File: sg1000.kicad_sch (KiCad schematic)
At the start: 77 parts, among them CN1 Conn_01x07_Female, J1 USB-B1HSB6, J2 RCJ-014, J3 RCJ-013, Q1 2n4401, Q1c1 2n3906, SW1 Pause Key, SW2 Power Toggle, SW3 Reset Key, U1 SG-1000-Cart, U100 74HCT574, U101 74HCT574, U102 74HCT574, U103 AS6C62256-DIP, U11 AS6C62256-DIP, U12 TMS9918A, U13 74LS139, U16 74LS32, U17 74LS14, U18 74LS257, U2 SG-1000-Expansion, U21 74LS257, U3 SN76489AN, U4 74LS32, U5 27C256, U6 74LS573, U7 74LS00, U9 Z80CPU, U99 74HCT04, X2 10.73863MHz

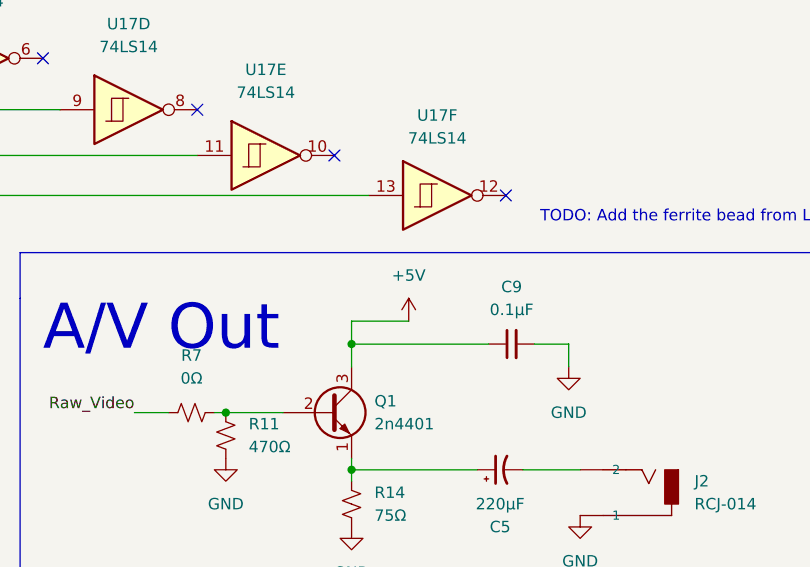
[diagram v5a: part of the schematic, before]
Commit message: Add ferrite bead to video path
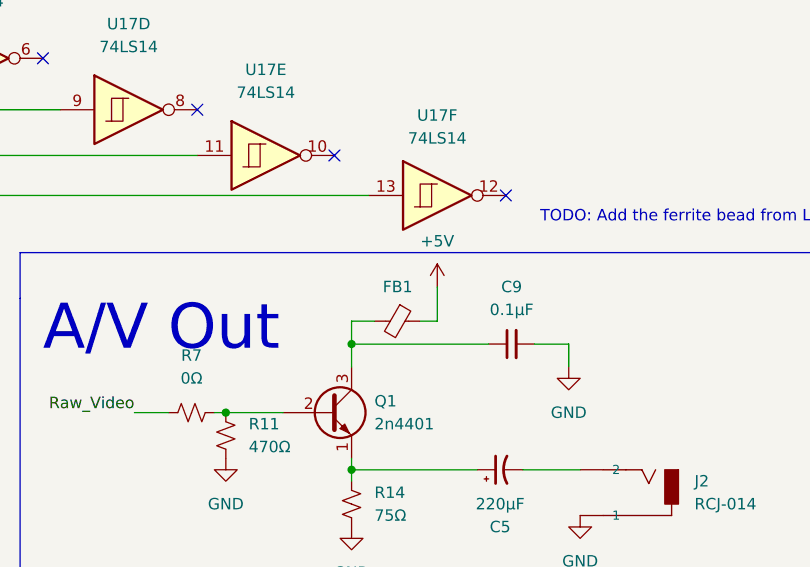
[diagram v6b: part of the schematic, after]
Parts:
- added FB1: FerriteBead_Small, Inductor_SMD:L_1206_3216Metric_Pad1.22x1.90mm_HandSolder, symbol Device:FerriteBead_Small
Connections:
- net +5V: now also FB1.1; no longer C9.1, Q1.3 (C)
- new net: C9.1, FB1.2, Q1.3 (C)
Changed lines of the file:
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@@
     (stroke (width 0) (type default) (color 0 0 0 0))
   )
-  (wire (pts (xy 290.83 165.1) (xy 284.48 165.1))
-    (stroke (width 0) (type default) (color 0 0 0 0))
-  )
   (wire (pts (xy 43.815 683.895) (xy 51.435 683.895))
     (stroke (width 0) (type default) (color 0 0 0 0))
@@
     (stroke (width 0) (type default) (color 0 0 0 0))
   )
+  (wire (pts (xy 294.005 165.1) (xy 294.005 161.29))
+    (stroke (width 0) (type default) (color 0 0 0 0))
+  )
   (wire (pts (xy 33.02 236.22) (xy 39.37 236.22))
     (stroke (width 0) (type default) (color 0 0 0 0))
@@
     (stroke (width 0) (type default) (color 0 0 0 0))
   )
+  (wire (pts (xy 292.1 165.1) (xy 294.005 165.1))
+    (stroke (width 0) (type default) (color 0 0 0 0))
+  )
   (wire (pts (xy 172.72 527.05) (xy 182.88 527.05))
     (stroke (width 0) (type default) (color 0 0 0 0))
@@
     (stroke (width 0) (type default) (color 0 0 0 0))
   )
+  (wire (pts (xy 284.48 165.1) (xy 287.02 165.1))
+    (stroke (width 0) (type default) (color 0 0 0 0))
+  )
   (wire (pts (xy 77.47 582.93) (xy 80.01 582.93))
     (stroke (width 0) (type default) (color 0 0 0 0))
@@
     (pin "1")
   )
+  (symbol (lib_id "Device:FerriteBead_Small") (at 289.56 165.1 270) (unit 1)
+    (in_bom yes) (on_board yes) (fields_autoplaced)
+    (property "Reference" "FB1" (id 0) (at 289.5981 161.29 90))
+    (property "Value" "FerriteBead_Small" (id 1) (at 289.5981 161.29 90)
+      (effects (font (size 1.27 1.27)) hide)
+    )
+    (property "Footprint" "Inductor_SMD:L_1206_3216Metric_Pad1.22x1.90mm_HandSolder" (id 2) (at 289.56 163.322 90)
+      (effects (font (size 1.27 1.27)) hide)
+    )
+    (property "Datasheet" "~" (id 3) (at 289.56 165.1 0)
+      (effects (font (size 1.27 1.27)) hide)
+    )
+    (property "DigiKey" "283-MFBW1V3216-310-RCT-ND" (id 4) (at 289.56 165.1 0)
+      (effects (font (size 1.27 1.27)) hide)
+    )
+    (pin "1")
+    (pin "2")
+  )
   (symbol (lib_id "Device:C_Trim_Small") (at 165.1 202.565 90) (unit 1)
     (in_bom yes) (on_board yes)
@@
     (pin "1")
   )
-  (symbol (lib_id "power:+5V") (at 290.83 165.1 0) (unit 1)
+  (symbol (lib_id "power:+5V") (at 294.005 161.29 0) (unit 1)
     (in_bom yes) (on_board yes) (fields_autoplaced)
-    (property "Reference" "#PWR0152" (id 0) (at 290.83 168.91 0)
+    (property "Reference" "#PWR0152" (id 0) (at 294.005 165.1 0)
       (effects (font (size 1.27 1.27)) hide)
     )
-    (property "Value" "+5V" (id 1) (at 290.83 160.02 0))
-    (property "Footprint" "" (id 2) (at 290.83 165.1 0)
+    (property "Value" "+5V" (id 1) (at 294.005 156.21 0))
+    (property "Footprint" "" (id 2) (at 294.005 161.29 0)
       (effects (font (size 1.27 1.27)) hide)
     )
-    (property "Datasheet" "" (id 3) (at 290.83 165.1 0)
+    (property "Datasheet" "" (id 3) (at 294.005 161.29 0)
       (effects (font (size 1.27 1.27)) hide)
     )
@@
       (reference "F1") (unit 1) (value "2A") (footprint "Fuse:Fuse_0805_2012Metric_Pad1.15x1.40mm_HandSolder")
     )
+    (path "/43869f2f-9cd6-4f1f-b6e4-613d616a6ac6"
+      (reference "FB1") (unit 1) (value "FerriteBead_Small") (footprint "Inductor_SMD:L_1206_3216Metric_Pad1.22x1.90mm_HandSolder")
+    )
     (path "/29d819aa-b433-48a1-9c7f-65135350c51c"

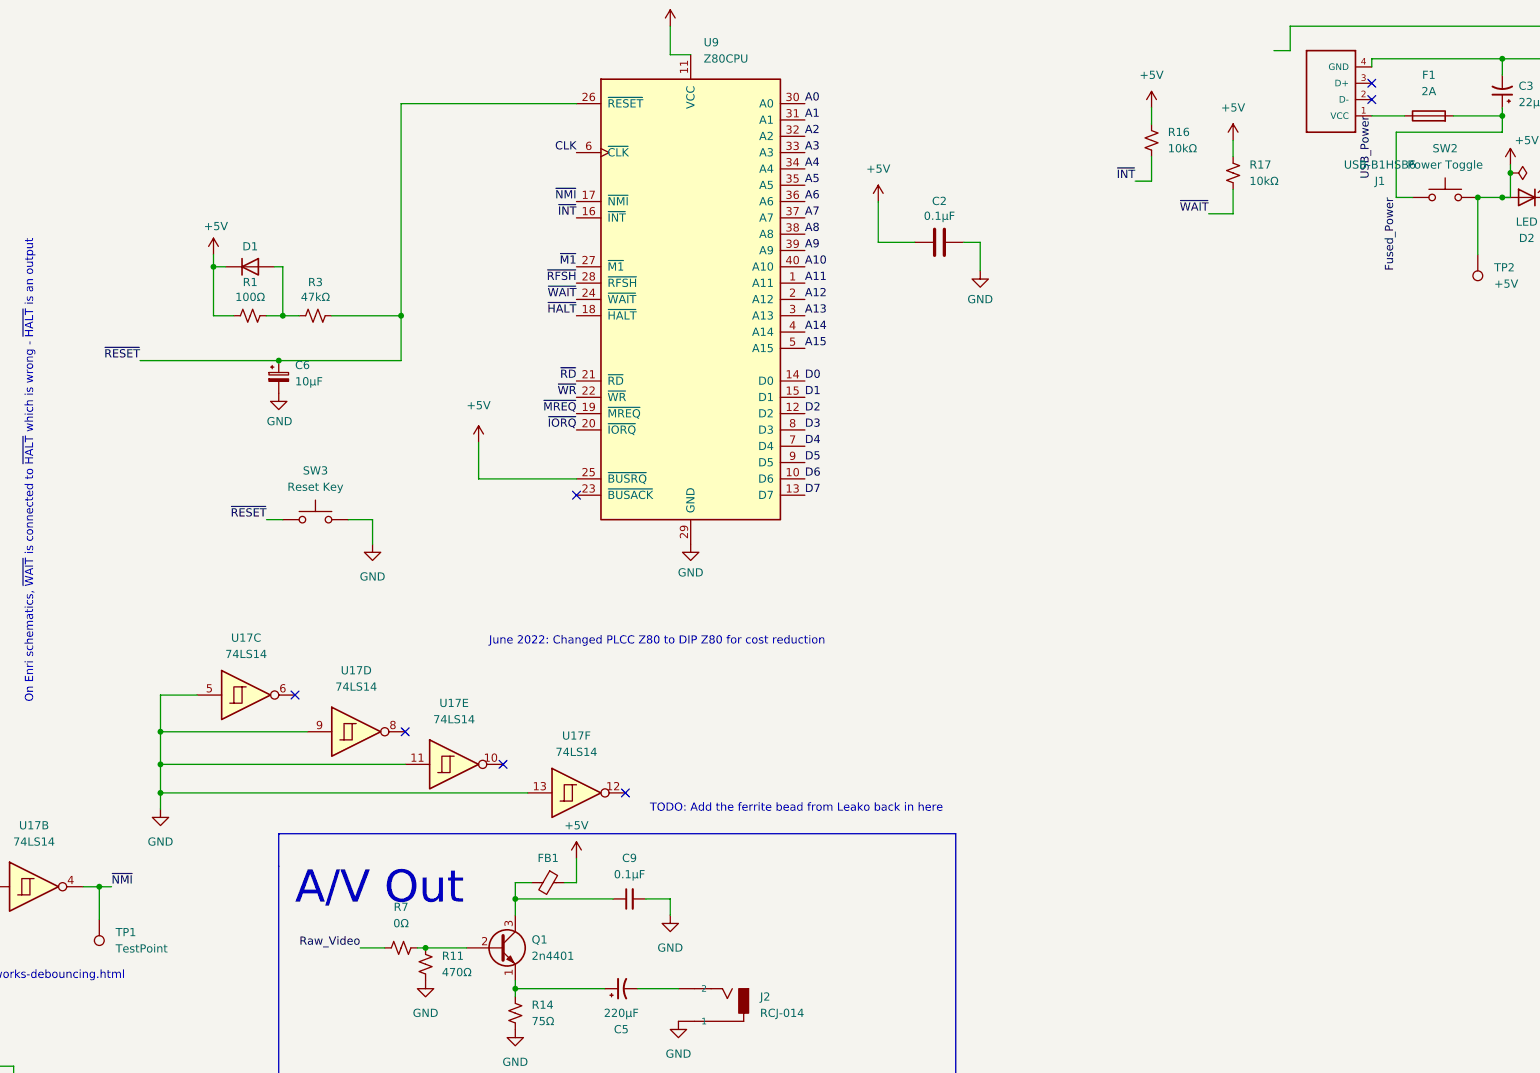
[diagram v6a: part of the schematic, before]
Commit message: Bigger test points for +5V and GND
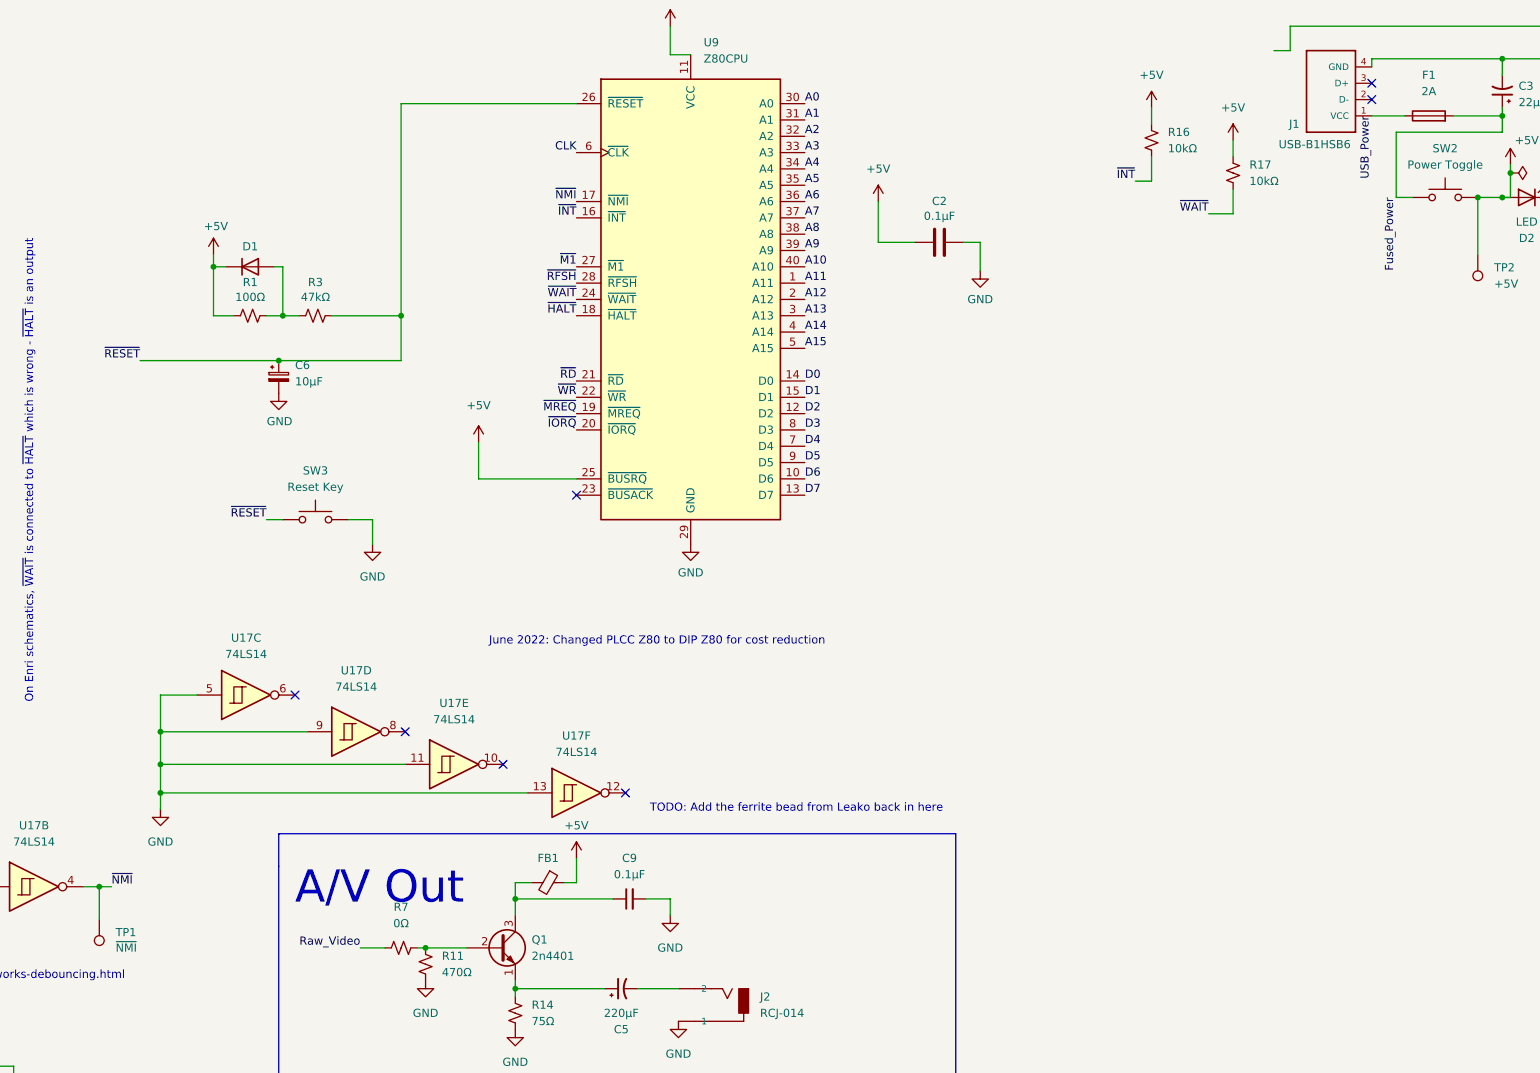
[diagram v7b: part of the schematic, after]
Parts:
- TP1: value TestPoint -> ~{NMI}
- TP2, TP3: footprint TestPoint:TestPoint_Loop_D1.80mm_Drill1.0mm_Beaded -> TestPoint:TestPoint_Loop_D2.50mm_Drill1.0mm
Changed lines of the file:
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@@
   )
   (symbol (lib_id "USB-B1HSB6:USB-B1HSB6") (at 415.29 43.18 180) (unit 1)
-    (in_bom yes) (on_board yes) (fields_autoplaced)
-    (property "Reference" "J1" (id 0) (at 419.1 55.88 0))
-    (property "Value" "USB-B1HSB6" (id 1) (at 419.1 53.34 0))
+    (in_bom yes) (on_board yes)
+    (property "Reference" "J1" (id 0) (at 405.765 46.99 0))
+    (property "Value" "USB-B1HSB6" (id 1) (at 408.94 50.165 0))
     (property "Footprint" "USB-B1HSB6:OST_USB-B1HSB6" (id 2) (at 415.29 43.18 0)
       (effects (font (size 1.27 1.27)) (justify left bottom) hide)
@@
       (effects (font (size 1.27 1.27)) (justify right))
     )
-    (property "Footprint" "TestPoint:TestPoint_Loop_D1.80mm_Drill1.0mm_Beaded" (id 2) (at 453.39 67.31 0)
+    (property "Footprint" "TestPoint:TestPoint_Loop_D2.50mm_Drill1.0mm" (id 2) (at 453.39 67.31 0)
       (effects (font (size 1.27 1.27)) hide)
     )
@@
   )
   (symbol (lib_id "Connector:TestPoint") (at 219.71 170.815 180) (unit 1)
-    (in_bom no) (on_board yes) (fields_autoplaced)
+    (in_bom no) (on_board yes)
     (property "Reference" "TP1" (id 0) (at 222.25 172.8469 0)
       (effects (font (size 1.27 1.27)) (justify right))
     )
-    (property "Value" "TestPoint" (id 1) (at 222.25 175.3869 0)
+    (property "Value" "~{NMI}" (id 1) (at 222.25 175.26 0)
       (effects (font (size 1.27 1.27)) (justify right))
     )
@@
       (effects (font (size 1.27 1.27)) (justify right))
     )
-    (property "Footprint" "TestPoint:TestPoint_Loop_D1.80mm_Drill1.0mm_Beaded" (id 2) (at 429.26 67.31 0)
+    (property "Footprint" "TestPoint:TestPoint_Loop_D2.50mm_Drill1.0mm" (id 2) (at 429.26 67.31 0)
       (effects (font (size 1.27 1.27)) hide)
     )
@@
     )
     (path "/f84a0f9f-b031-4fe7-8478-dc5d7b9d04c7"
-      (reference "TP1") (unit 1) (value "TestPoint") (footprint "TestPoint:TestPoint_Loop_D2.50mm_Drill1.0mm")
+      (reference "TP1") (unit 1) (value "~{NMI}") (footprint "TestPoint:TestPoint_Loop_D2.50mm_Drill1.0mm")
     )
     (path "/ffc04502-f2c9-488f-b0ef-6c293c75f8de"
-      (reference "TP2") (unit 1) (value "+5V") (footprint "TestPoint:TestPoint_Loop_D1.80mm_Drill1.0mm_Beaded")
+      (reference "TP2") (unit 1) (value "+5V") (footprint "TestPoint:TestPoint_Loop_D2.50mm_Drill1.0mm")
     )
     (path "/bc415191-2264-432a-91a2-21b0cf8e7e17"
-      (reference "TP3") (unit 1) (value "GND") (footprint "TestPoint:TestPoint_Loop_D1.80mm_Drill1.0mm_Beaded")
+      (reference "TP3") (unit 1) (value "GND") (footprint "TestPoint:TestPoint_Loop_D2.50mm_Drill1.0mm")
     )
     (path "/e4e9a9cd-894c-43a6-bbd2-9190e99d71d4"

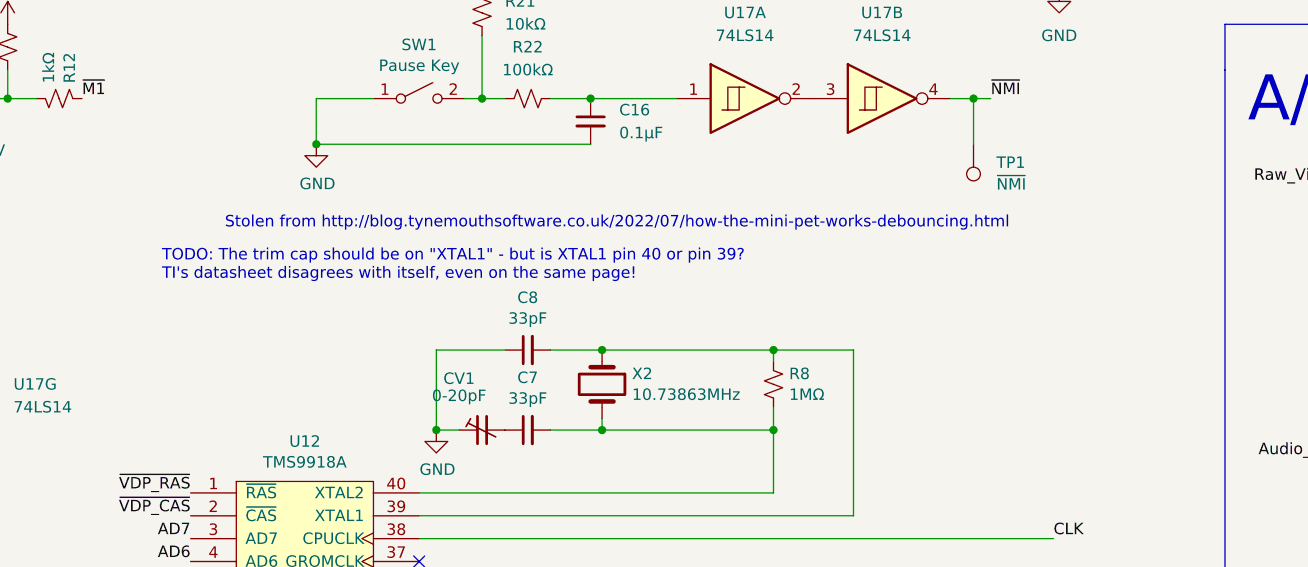
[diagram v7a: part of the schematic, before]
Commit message: XTAL1 mystery solved
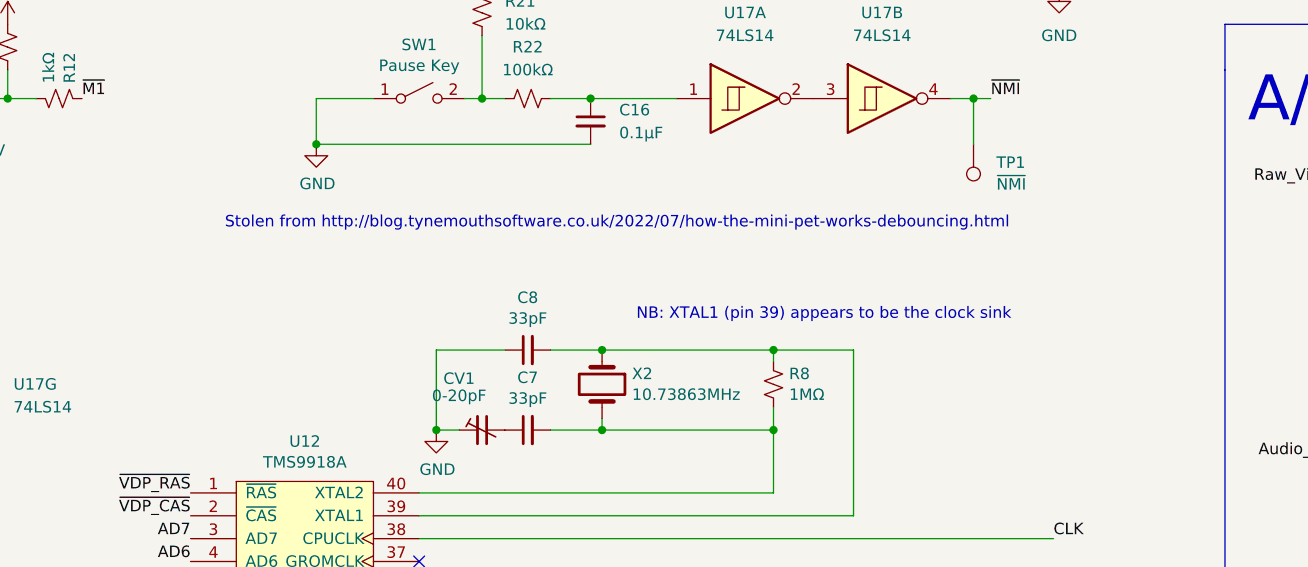
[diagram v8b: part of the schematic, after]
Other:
- note added: "NB: XTAL1 (pin 39) appears to be the clock sink"
- note removed: "TODO: The trim cap should be on "XTAL1" - but is XTAL1 pin 40 or pin 39? TI's datasheet disagrees with itself, even on the same page!"
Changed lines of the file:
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@@
     (effects (font (size 5.0038 5.0038)) (justify left bottom))
   )
-  (text "TODO: The trim cap should be on \"XTAL1\" - but is XTAL1 pin 40 or pin 39?\nTI's datasheet disagrees with itself, even on the same page!"
-    (at 129.54 186.055 0)
+  (text "NB: XTAL1 (pin 39) appears to be the clock sink" (at 182.245 190.5 0)
     (effects (font (size 1.27 1.27)) (justify left bottom))
   )
